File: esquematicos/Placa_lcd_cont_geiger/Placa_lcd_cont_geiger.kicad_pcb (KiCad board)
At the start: 2 copper layers, 68.6 x 53.3 mm, 17 parts, among them J1 Conn_02x04_Counter_Clockwise, J2 Conn_01x14_Female, J3 Conn_01x04_Female, P1 Power, P2 Analog, P3 Digital, P4 Digital, Q1 BC548, Q2 BC548

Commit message: Agregado del PCB del teclado(2)
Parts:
- J3: footprint Connector_JST:JST_EH_B04B-EH-A_1x04_P2.50mm_Vertical -> Connector_JST:JST_XH_B04B-XH-A_1x04_P2.50mm_Vertical
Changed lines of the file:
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@@
   )
   (setup
-    (last_trace_width 1.27)
+    (last_trace_width 0.25)
     (user_trace_width 1.016)
     (user_trace_width 1.27)
@@
     )
   )
-  (module Connector_JST:JST_EH_B04B-EH-A_1x04_P2.50mm_Vertical (layer F.Cu)
-    (at 162.052 115.697 180)
-    (descr "JST EH series connector, B04B-EH-A (http://www.jst-mfg.com/product/pdf/eng/eEH.pdf), generated with kicad-footprint-generator")
-    (tags "connector JST EH side entry")
-    (fp_text reference J3 (at 3.75 -2.8 180) (layer F.SilkS)
-      (effects (font (size 1 1) (thickness 0.15)))
-    )
-    (fp_text value Conn_01x04_Female (at 3.75 3.4 180) (layer F.Fab)
-      (effects (font (size 1 1) (thickness 0.15)))
-    )
-    (fp_line (start -2.5 -1.6) (end -2.5 2.2) (layer F.Fab) (width 0.1))
-    (fp_line (start -2.5 2.2) (end 10 2.2) (layer F.Fab) (width 0.1))
-    (fp_line (start 10 2.2) (end 10 -1.6) (layer F.Fab) (width 0.1))
-    (fp_line (start 10 -1.6) (end -2.5 -1.6) (layer F.Fab) (width 0.1))
-    (fp_line (start -3 -2.1) (end -3 2.7) (layer F.CrtYd) (width 0.05))
-    (fp_line (start -3 2.7) (end 10.5 2.7) (layer F.CrtYd) (width 0.05))
-    (fp_line (start 10.5 2.7) (end 10.5 -2.1) (layer F.CrtYd) (width 0.05))
-    (fp_line (start 10.5 -2.1) (end -3 -2.1) (layer F.CrtYd) (width 0.05))
-    (fp_line (start -2.61 -1.71) (end -2.61 2.31) (layer F.SilkS) (width 0.12))
-    (fp_line (start -2.61 2.31) (end 10.11 2.31) (layer F.SilkS) (width 0.12))
-    (fp_line (start 10.11 2.31) (end 10.11 -1.71) (layer F.SilkS) (width 0.12))
-    (fp_line (start 10.11 -1.71) (end -2.61 -1.71) (layer F.SilkS) (width 0.12))
-    (fp_line (start -2.61 0) (end -2.11 0) (layer F.SilkS) (width 0.12))
-    (fp_line (start -2.11 0) (end -2.11 -1.21) (layer F.SilkS) (width 0.12))
-    (fp_line (start -2.11 -1.21) (end 9.61 -1.21) (layer F.SilkS) (width 0.12))
-    (fp_line (start 9.61 -1.21) (end 9.61 0) (layer F.SilkS) (width 0.12))
-    (fp_line (start 9.61 0) (end 10.11 0) (layer F.SilkS) (width 0.12))
-    (fp_line (start -2.61 0.81) (end -1.61 0.81) (layer F.SilkS) (width 0.12))
-    (fp_line (start -1.61 0.81) (end -1.61 2.31) (layer F.SilkS) (width 0.12))
-    (fp_line (start 10.11 0.81) (end 9.11 0.81) (layer F.SilkS) (width 0.12))
-    (fp_line (start 9.11 0.81) (end 9.11 2.31) (layer F.SilkS) (width 0.12))
-    (fp_line (start -2.91 0.11) (end -2.91 2.61) (layer F.SilkS) (width 0.12))
-    (fp_line (start -2.91 2.61) (end -0.41 2.61) (layer F.SilkS) (width 0.12))
-    (fp_line (start -2.91 0.11) (end -2.91 2.61) (layer F.Fab) (width 0.1))
-    (fp_line (start -2.91 2.61) (end -0.41 2.61) (layer F.Fab) (width 0.1))
-    (fp_text user %R (at 3.75 1.5 180) (layer F.Fab)
-      (effects (font (size 1 1) (thickness 0.15)))
-    )
-    (pad 1 thru_hole roundrect (at 0 0 180) (size 1.7 1.95) (drill 0.95) (layers *.Cu *.Mask) (roundrect_rratio 0.147059)
-      (net 35 "Net-(J3-Pad1)"))
-    (pad 2 thru_hole oval (at 2.5 0 180) (size 1.7 1.95) (drill 0.95) (layers *.Cu *.Mask)
-      (net 5 /A0))
-    (pad 3 thru_hole oval (at 5 0 180) (size 1.7 1.95) (drill 0.95) (layers *.Cu *.Mask)
-      (net 3 GND))
-    (pad 4 thru_hole oval (at 7.5 0 180) (size 1.7 1.95) (drill 0.95) (layers *.Cu *.Mask)
-      (net 30 VCC))
-    (model ${KISYS3DMOD}/Connector_JST.3dshapes/JST_EH_B04B-EH-A_1x04_P2.50mm_Vertical.wrl
-      (at (xyz 0 0 0))
-      (scale (xyz 1 1 1))
-      (rotate (xyz 0 0 0))
-    )
-  )
   (module Package_TO_SOT_THT:TO-92_Inline (layer F.Cu)
     (at 144.78 114.427)
@@
       (at (xyz 0 0 0))
       (scale (xyz 1 1 1))
+      (rotate (xyz 0 0 0))
+    )
+  )
+  (module Connector_JST:JST_XH_B04B-XH-A_1x04_P2.50mm_Vertical (layer F.Cu)
+    (at 162.052 115.697 180)
+    (descr "JST XH series connector, B04B-XH-A (http://www.jst-mfg.com/product/pdf/eng/eXH.pdf), generated with kicad-footprint-generator")
+    (tags "connector JST XH side entry")
+    (fp_text reference J3 (at 3.75 -3.55 180) (layer F.SilkS)
+      (effects (font (size 1 1) (thickness 0.15)))
+    )
+    (fp_text value Conn_01x04_Female (at 3.75 4.6 180) (layer F.Fab)
+      (effects (font (size 1 1) (thickness 0.15)))
+    )
+    (fp_line (start -2.45 -2.35) (end -2.45 3.4) (layer F.Fab) (width 0.1))
+    (fp_line (start -2.45 3.4) (end 9.95 3.4) (layer F.Fab) (width 0.1))
+    (fp_line (start 9.95 3.4) (end 9.95 -2.35) (layer F.Fab) (width 0.1))
+    (fp_line (start 9.95 -2.35) (end -2.45 -2.35) (layer F.Fab) (width 0.1))
+    (fp_line (start -2.56 -2.46) (end -2.56 3.51) (layer F.SilkS) (width 0.12))
+    (fp_line (start -2.56 3.51) (end 10.06 3.51) (layer F.SilkS) (width 0.12))
+    (fp_line (start 10.06 3.51) (end 10.06 -2.46) (layer F.SilkS) (width 0.12))
+    (fp_line (start 10.06 -2.46) (end -2.56 -2.46) (layer F.SilkS) (width 0.12))
+    (fp_line (start -2.95 -2.85) (end -2.95 3.9) (layer F.CrtYd) (width 0.05))
+    (fp_line (start -2.95 3.9) (end 10.45 3.9) (layer F.CrtYd) (width 0.05))
+    (fp_line (start 10.45 3.9) (end 10.45 -2.85) (layer F.CrtYd) (width 0.05))
+    (fp_line (start 10.45 -2.85) (end -2.95 -2.85) (layer F.CrtYd) (width 0.05))
+    (fp_line (start -0.625 -2.35) (end 0 -1.35) (layer F.Fab) (width 0.1))
+    (fp_line (start 0 -1.35) (end 0.625 -2.35) (layer F.Fab) (width 0.1))
+    (fp_line (start 0.75 -2.45) (end 0.75 -1.7) (layer F.SilkS) (width 0.12))
+    (fp_line (start 0.75 -1.7) (end 6.75 -1.7) (layer F.SilkS) (width 0.12))
+    (fp_line (start 6.75 -1.7) (end 6.75 -2.45) (layer F.SilkS) (width 0.12))
+    (fp_line (start 6.75 -2.45) (end 0.75 -2.45) (layer F.SilkS) (width 0.12))
+    (fp_line (start -2.55 -2.45) (end -2.55 -1.7) (layer F.SilkS) (width 0.12))
+    (fp_line (start -2.55 -1.7) (end -0.75 -1.7) (layer F.SilkS) (width 0.12))
+    (fp_line (start -0.75 -1.7) (end -0.75 -2.45) (layer F.SilkS) (width 0.12))
+    (fp_line (start -0.75 -2.45) (end -2.55 -2.45) (layer F.SilkS) (width 0.12))
+    (fp_line (start 8.25 -2.45) (end 8.25 -1.7) (layer F.SilkS) (width 0.12))
+    (fp_line (start 8.25 -1.7) (end 10.05 -1.7) (layer F.SilkS) (width 0.12))
+    (fp_line (start 10.05 -1.7) (end 10.05 -2.45) (layer F.SilkS) (width 0.12))
+    (fp_line (start 10.05 -2.45) (end 8.25 -2.45) (layer F.SilkS) (width 0.12))
+    (fp_line (start -2.55 -0.2) (end -1.8 -0.2) (layer F.SilkS) (width 0.12))
+    (fp_line (start -1.8 -0.2) (end -1.8 2.75) (layer F.SilkS) (width 0.12))
+    (fp_line (start -1.8 2.75) (end 3.75 2.75) (layer F.SilkS) (width 0.12))
+    (fp_line (start 10.05 -0.2) (end 9.3 -0.2) (layer F.SilkS) (width 0.12))
+    (fp_line (start 9.3 -0.2) (end 9.3 2.75) (layer F.SilkS) (width 0.12))
+    (fp_line (start 9.3 2.75) (end 3.75 2.75) (layer F.SilkS) (width 0.12))
+    (fp_line (start -1.6 -2.75) (end -2.85 -2.75) (layer F.SilkS) (width 0.12))
+    (fp_line (start -2.85 -2.75) (end -2.85 -1.5) (layer F.SilkS) (width 0.12))
+    (fp_text user %R (at 3.75 2.7 180) (layer F.Fab)
+      (effects (font (size 1 1) (thickness 0.15)))
+    )
+    (pad 1 thru_hole roundrect (at 0 0 180) (size 1.7 1.95) (drill 0.95) (layers *.Cu *.Mask) (roundrect_rratio 0.147059)
+      (net 35 "Net-(J3-Pad1)"))
+    (pad 2 thru_hole oval (at 2.5 0 180) (size 1.7 1.95) (drill 0.95) (layers *.Cu *.Mask)
+      (net 5 /A0))
+    (pad 3 thru_hole oval (at 5 0 180) (size 1.7 1.95) (drill 0.95) (layers *.Cu *.Mask)
+      (net 3 GND))
+    (pad 4 thru_hole oval (at 7.5 0 180) (size 1.7 1.95) (drill 0.95) (layers *.Cu *.Mask)
+      (net 30 VCC))
+    (model ${KISYS3DMOD}/Connector_JST.3dshapes/JST_XH_B04B-XH-A_1x04_P2.50mm_Vertical.wrl
+      (at (xyz 0 0 0))
+      (scale (xyz 1 1 1))

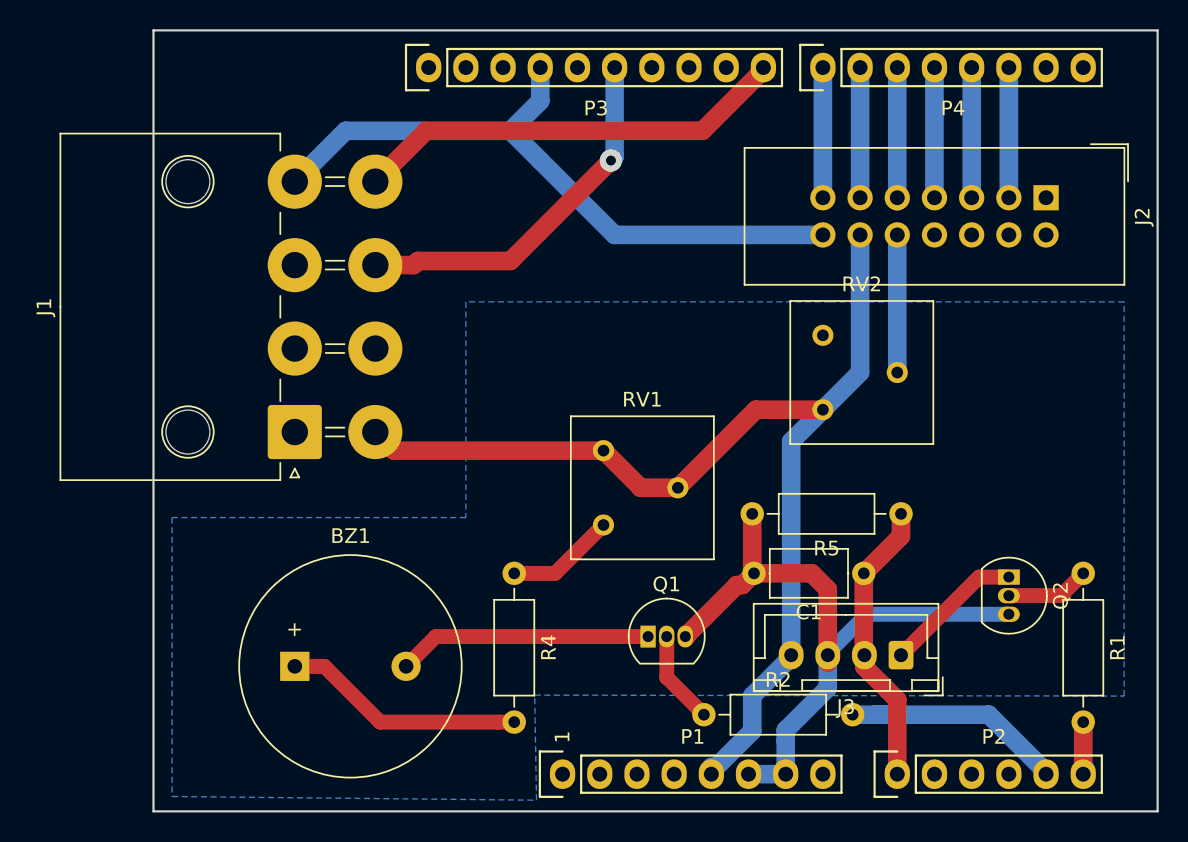
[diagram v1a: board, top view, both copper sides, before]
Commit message: Agregado de LED verde a la placa del teclado e incremento de las dimensiones de esta última incluyendo una mayor separación entre los botones
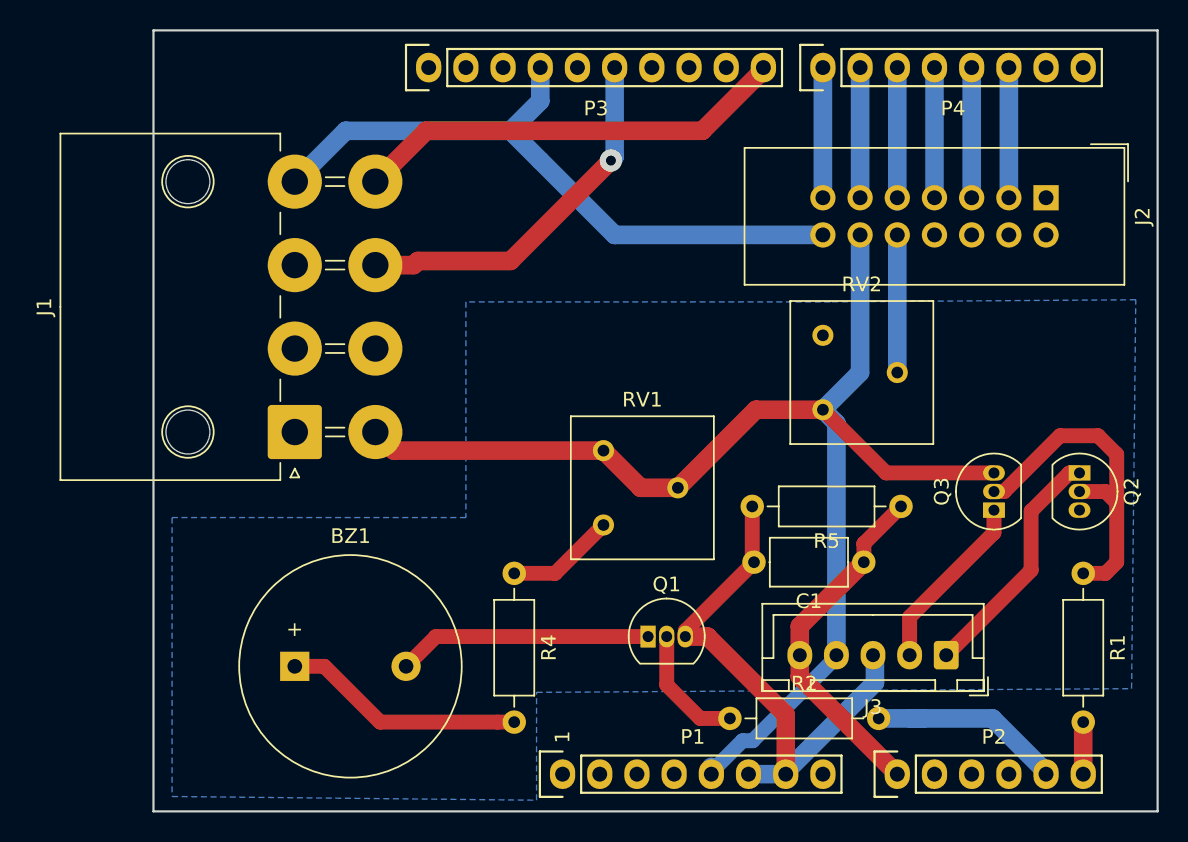
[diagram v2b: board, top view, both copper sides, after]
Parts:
- added Q3: BC558, Package_TO_SOT_THT:TO-92_Inline, F.Cu at (168.4, 105.8)
- J3: value Conn_01x04_Female -> Conn_01x05_Female; footprint Connector_JST:JST_XH_B04B-XH-A_1x04_P2.50mm_Vertical -> Connector_JST:JST_XH_B05B-XH-A_1x05_P2.50mm_Vertical
- moved Q2 8.59 mm to (174.2, 103.3)
- moved J3 3.09 mm to (165.1, 115.7)
- moved R2 1.80 mm to (150.4, 120.0)
- moved C1 0.76 mm to (159.5, 109.3)
- moved R5 0.51 mm to (162.1, 105.5)
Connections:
- J3 pad 2: /A0 -> Net-(J3-Pad2)
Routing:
- net Net-(Q2-Pad2): track 5.71 -> 23.3 mm
- net VCC: track 76.0 -> 90.9 mm
- net Net-(J3-Pad2): track 0.00 -> 12.4 mm
- net GND: track 92.3 -> 83.5 mm
- net Net-(J3-Pad1): track 9.58 -> 16.6 mm
- net /A0: track 19.9 -> 24.1 mm
- net Net-(Q1-Pad2): track 6.39 -> 8.57 mm
- net /A4: track 16.1 -> 14.0 mm

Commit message: Agrega PCB del teclado
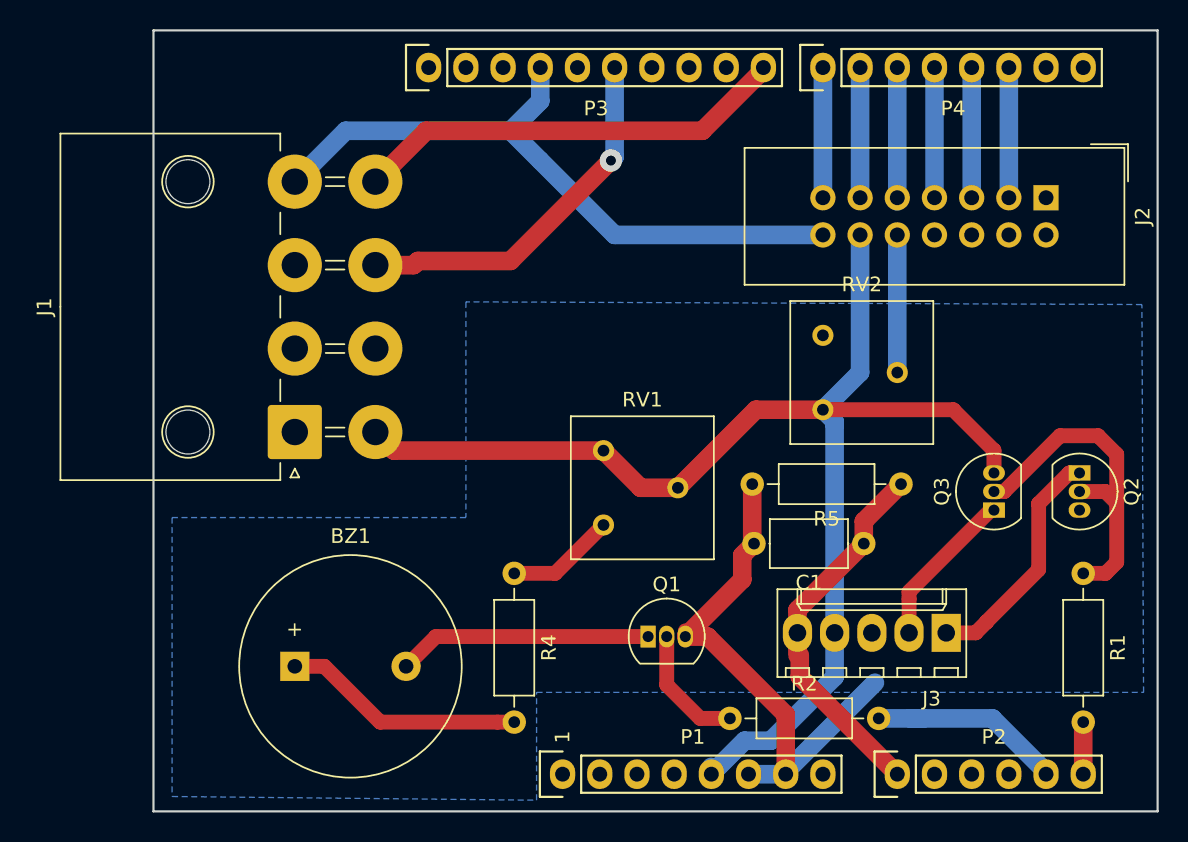
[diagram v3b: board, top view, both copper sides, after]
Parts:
- J3: footprint Connector_JST:JST_XH_B05B-XH-A_1x05_P2.50mm_Vertical -> Connectors_Molex:Molex_KK-6410-05_05x2.54mm_Straight
- moved J3 1.52 mm to (165.1, 114.2)
- moved R5 1.52 mm to (162.1, 104.0)
- moved C1 1.27 mm to (159.5, 108.1)
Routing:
- net /A0: track 24.1 -> 25.7 mm
- net Net-(J3-Pad2): track 12.4 -> 10.9 mm
- net VCC: track 90.9 -> 92.1 mm
